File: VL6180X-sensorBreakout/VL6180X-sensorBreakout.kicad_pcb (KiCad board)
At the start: 2 copper layers, 17.8 x 16.3 mm, 8 parts, among them P1 CONN_6, U1 VL6180X

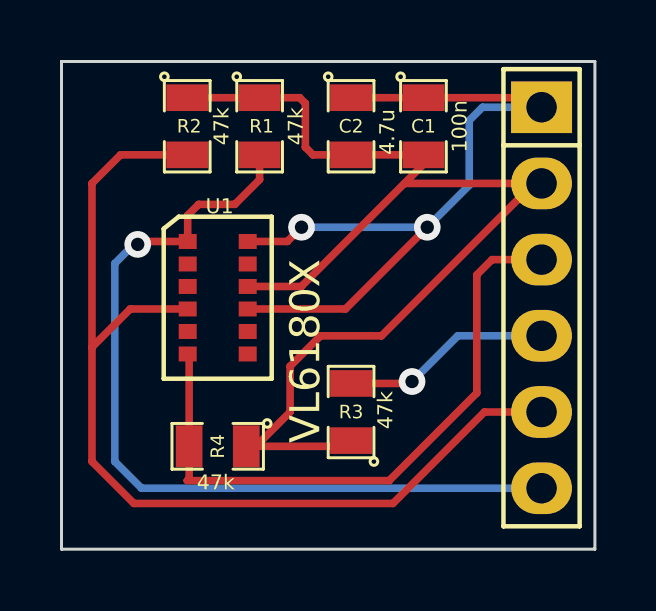
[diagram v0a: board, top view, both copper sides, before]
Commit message: added missing trace
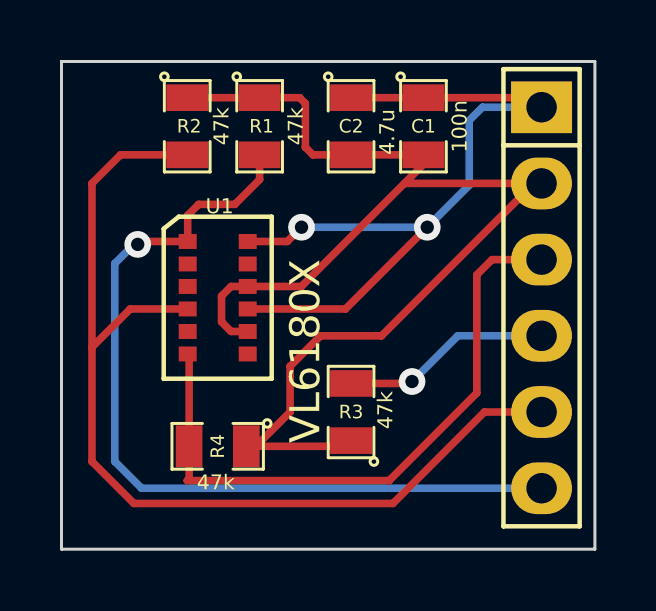
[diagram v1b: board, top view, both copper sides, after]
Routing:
- net VCC: track 40.5 -> 43.4 mm
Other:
- board text added: "GND"
- board text added: "GPIO0"
- board text added: "GPIO1"
- board text added: "SCL"
- board text added: "SDA"
- board text added: "Vcc"
